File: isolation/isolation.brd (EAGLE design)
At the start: 74.5 x 72.7 mm, 81 parts, among them IC1 XTLV61048DBVR, IC2 SN74HC14PWR, IC3 SN74HCS32BQAR, IC4 SN74HCS08DYYR, IC5 FDN359BN, IC6 FDN359BN, IC7 FDN359BN, IC8 FDN359BN, J1 S4B-PH-K-S(LF)(SN), J2 S4B-PH-K-S(LF)(SN), J3 S4B-PH-K-S(LF)(SN), J4 S4B-PH-K-S(LF)(SN), J5 S4B-PH-K-S(LF)(SN)

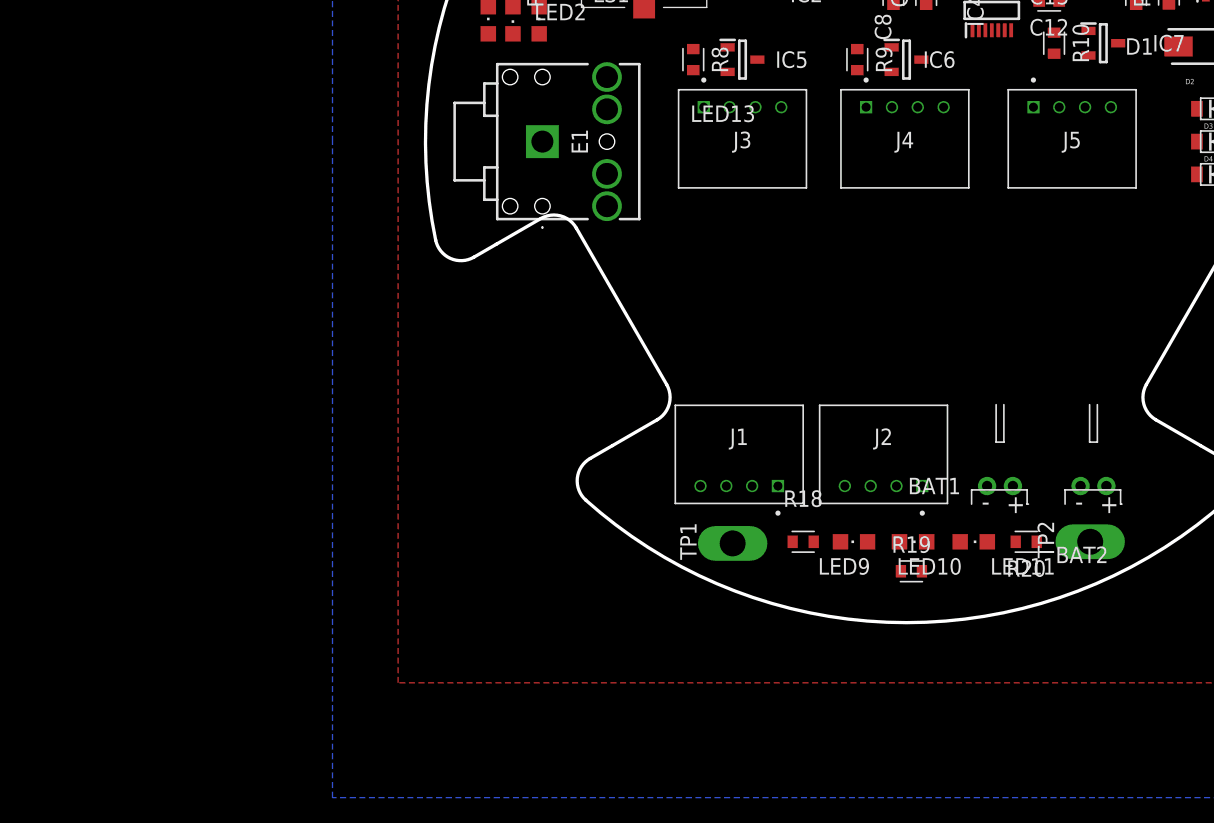
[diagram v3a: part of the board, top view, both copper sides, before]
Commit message: 2 pin ignitor connectors
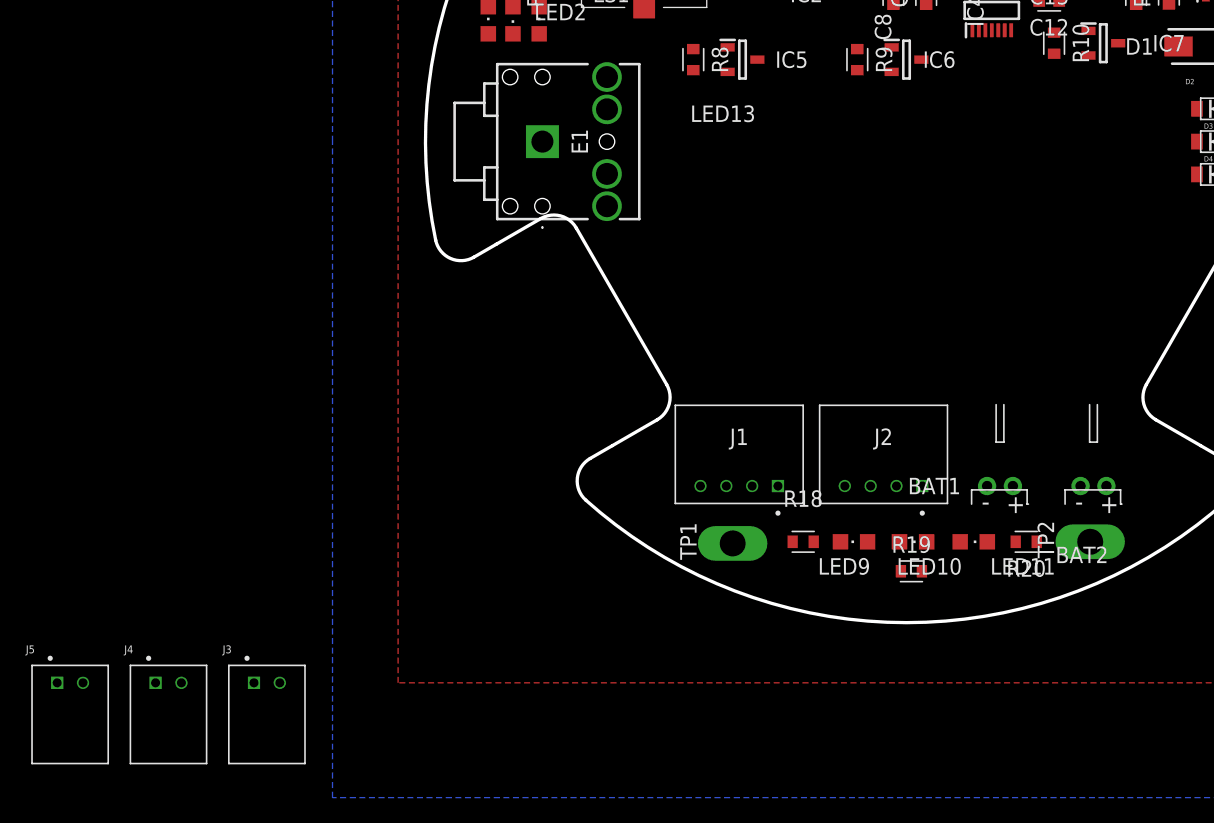
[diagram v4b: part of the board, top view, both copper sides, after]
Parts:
- J3, J4, J5: value S4B-PH-K-S(LF)(SN) -> S2B-PH-K-S(LF)(SN); device Headers:S4B-PH-K-S(LF)(SN) -> Connectors:S2B-PH-K-S(LF)(SN)
- moved J5 89.5 mm to (-64.8, -41.9)
- moved J4 72.4 mm to (-57.1, -41.9)
- moved J3 57.8 mm to (-49.5, -41.9)
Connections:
- removed net N$19: IC6.3, J4.2, J4.3
- removed net N$20: IC7.3, J5.2, J5.3
- new net N$14: IC7.3, J5.2
- new net N$15: IC6.3, J4.2
- net N$17: no longer J3.3
- net VDEP: no longer J3.4, J4.4, J5.4
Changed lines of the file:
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@@
 <attribute name="VALUE" x="-20.32" y="25.4" size="1.27" layer="27" rot="R180" align="center"/>
-</element>
-<element name="J3" library="Headers" library_urn="urn:adsk.eagle:library:11687645" package="S4B-PH-K-S(LF)(SN)" package3d_urn="urn:adsk.eagle:package:19181369/5" value="S4B-PH-K-S(LF)(SN)" x="-12.7" y="2.667" smashed="yes">
-<attribute name="CREATED_BY" value="PCBLayout.com" x="-12.7" y="2.667" size="1.778" layer="27" display="off"/>
-<attribute name="DIGIKEY_PARTNO" value="455-1721-ND" x="-12.7" y="2.667" size="1.778" layer="27" display="off"/>
-<attribute name="MANUFACTURER" value="JST Sales America Inc." x="-12.7" y="2.667" size="1.778" layer="27" display="off"/>
-<attribute name="MPN" value="S4B-PH-K-S(LF)(SN)" x="-12.7" y="2.667" size="1.778" layer="27" display="off"/>
-<attribute name="NAME" x="-12.700003125" y="0.127003125" size="1.27" layer="25" align="center"/>
-<attribute name="VALUE" x="-12.7" y="2.667" size="1.27" layer="27" align="center"/>
-</element>
-<element name="J4" library="Headers" library_urn="urn:adsk.eagle:library:11687645" package="S4B-PH-K-S(LF)(SN)" package3d_urn="urn:adsk.eagle:package:19181369/5" value="S4B-PH-K-S(LF)(SN)" x="-0.127" y="2.667" smashed="yes">
-<attribute name="CREATED_BY" value="PCBLayout.com" x="-0.127" y="2.667" size="1.778" layer="27" display="off"/>
-<attribute name="DIGIKEY_PARTNO" value="455-1721-ND" x="-0.127" y="2.667" size="1.778" layer="27" display="off"/>
-<attribute name="MANUFACTURER" value="JST Sales America Inc." x="-0.127" y="2.667" size="1.778" layer="27" display="off"/>
-<attribute name="MPN" value="S4B-PH-K-S(LF)(SN)" x="-0.127" y="2.667" size="1.778" layer="27" display="off"/>
-<attribute name="NAME" x="-0.127003125" y="0.127003125" size="1.27" layer="25" align="center"/>
-<attribute name="VALUE" x="-0.127" y="2.667" size="1.27" layer="27" align="center"/>
-</element>
-<element name="J5" library="Headers" library_urn="urn:adsk.eagle:library:11687645" package="S4B-PH-K-S(LF)(SN)" package3d_urn="urn:adsk.eagle:package:19181369/5" value="S4B-PH-K-S(LF)(SN)" x="12.827" y="2.667" smashed="yes">
-<attribute name="CREATED_BY" value="PCBLayout.com" x="12.827" y="2.667" size="1.778" layer="27" display="off"/>
-<attribute name="DIGIKEY_PARTNO" value="455-1721-ND" x="12.827" y="2.667" size="1.778" layer="27" display="off"/>
-<attribute name="MANUFACTURER" value="JST Sales America Inc." x="12.827" y="2.667" size="1.778" layer="27" display="off"/>
-<attribute name="MPN" value="S4B-PH-K-S(LF)(SN)" x="12.827" y="2.667" size="1.778" layer="27" display="off"/>
-<attribute name="NAME" x="12.826996875" y="0.127003125" size="1.27" layer="25" align="center"/>
-<attribute name="VALUE" x="12.827" y="2.667" size="1.27" layer="27" align="center"/>
 </element>
 <element name="R8" library="Resistor" library_urn="urn:adsk.eagle:library:16378527" package="RESC1608X60" package3d_urn="urn:adsk.eagle:package:16378565/5" value="68k" x="-16.51" y="6.35" smashed="yes" rot="R270">
@@
 <attribute name="TP_SIGNAL_NAME" value="" x="14.224" y="-30.988" size="1.778" layer="27" font="vector" rot="R90" display="off"/>
 <attribute name="VALUE" x="14.224" y="-30.988" size="0.0254" layer="27" rot="R90"/>
+</element>
+<element name="J3" library="Connectors" library_urn="urn:adsk.eagle:library:14555660" package="S2B-PH-K-S(LF)(SN)" package3d_urn="urn:adsk.eagle:package:10989924/2" value="S2B-PH-K-S(LF)(SN)" x="-49.53" y="-41.91" smashed="yes">
+<attribute name="CREATED_BY" value="PCBLayout.com" x="-49.53" y="-41.91" size="1.778" layer="27" display="off"/>
+<attribute name="DIGI_KEY_PART_NUMBER" value="455-1719-ND" x="-49.53" y="-41.91" size="1.778" layer="27" display="off"/>
+<attribute name="MANUFACTURER" value="JST Sales America Inc." x="-49.53" y="-41.91" size="1.778" layer="27" display="off"/>
+<attribute name="MPN" value="S2B-PH-K-S(LF)(SN)" x="-49.53" y="-41.91" size="1.778" layer="27" display="off"/>
+<attribute name="NAME" x="-52.959" y="-39.624" size="0.6096" layer="25"/>
+<attribute name="VALUE" x="-52.83" y="-49.11" size="0.6096" layer="27"/>
+</element>
+<element name="J4" library="Connectors" library_urn="urn:adsk.eagle:library:14555660" package="S2B-PH-K-S(LF)(SN)" package3d_urn="urn:adsk.eagle:package:10989924/2" value="S2B-PH-K-S(LF)(SN)" x="-57.15" y="-41.91" smashed="yes">
+<attribute name="CREATED_BY" value="PCBLayout.com" x="-57.15" y="-41.91" size="1.778" layer="27" display="off"/>
+<attribute name="DIGI_KEY_PART_NUMBER" value="455-1719-ND" x="-57.15" y="-41.91" size="1.778" layer="27" display="off"/>
+<attribute name="MANUFACTURER" value="JST Sales America Inc." x="-57.15" y="-41.91" size="1.778" layer="27" display="off"/>
+<attribute name="MPN" value="S2B-PH-K-S(LF)(SN)" x="-57.15" y="-41.91" size="1.778" layer="27" display="off"/>
+<attribute name="NAME" x="-60.579" y="-39.624" size="0.6096" layer="25"/>
+<attribute name="VALUE" x="-60.45" y="-49.11" size="0.6096" layer="27"/>
+</element>
+<element name="J5" library="Connectors" library_urn="urn:adsk.eagle:library:14555660" package="S2B-PH-K-S(LF)(SN)" package3d_urn="urn:adsk.eagle:package:10989924/2" value="S2B-PH-K-S(LF)(SN)" x="-64.77" y="-41.91" smashed="yes">
+<attribute name="CREATED_BY" value="PCBLayout.com" x="-64.77" y="-41.91" size="1.778" layer="27" display="off"/>
+<attribute name="DIGI_KEY_PART_NUMBER" value="455-1719-ND" x="-64.77" y="-41.91" size="1.778" layer="27" display="off"/>
+<attribute name="MANUFACTURER" value="JST Sales America Inc." x="-64.77" y="-41.91" size="1.778" layer="27" display="off"/>
+<attribute name="MPN" value="S2B-PH-K-S(LF)(SN)" x="-64.77" y="-41.91" size="1.778" layer="27" display="off"/>
+<attribute name="NAME" x="-68.199" y="-39.624" size="0.6096" layer="25"/>
+<attribute name="VALUE" x="-68.07" y="-49.11" size="0.6096" layer="27"/>
 </element>
 </elements>
@@
 <contactref element="R2" pad="1"/>
 <contactref element="LS1" pad="1"/>
-<contactref element="J3" pad="4"/>
 <contactref element="J3" pad="1"/>
-<contactref element="J4" pad="4"/>
-<contactref element="J5" pad="4"/>
+<contactref element="J4" pad="1"/>
 <contactref element="J5" pad="1"/>
-<contactref element="J4" pad="1"/>
-<wire x1="17.78" y1="10.6554" x2="20.32" y2="10.6148" width="0" layer="19" extent="1-1"/>
+<wire x1="-58.15" y1="-41.91" x2="-65.77" y2="-41.91" width="0" layer="19" extent="1-1"/>
+<wire x1="-50.53" y1="-41.91" x2="-58.15" y2="-41.91" width="0" layer="19" extent="1-1"/>
+<wire x1="-20.32" y1="10.29" x2="-50.53" y2="-41.91" width="0" layer="19" extent="1-1"/>
+<wire x1="17.78" y1="10.6554" x2="-20.32" y2="10.29" width="0" layer="19" extent="1-1"/>
+<wire x1="20.32" y1="10.6148" x2="17.78" y2="10.6554" width="0" layer="19" extent="1-1"/>
 <wire x1="21.064" y1="7.366" x2="20.32" y2="10.6148" width="0" layer="19" extent="1-1"/>
-<wire x1="15.827" y1="2.667" x2="21.064" y2="7.366" width="0" layer="19" extent="1-1"/>
-<wire x1="9.827" y1="2.667" x2="15.827" y2="2.667" width="0" layer="19" extent="1-1"/>
-<wire x1="2.873" y1="2.667" x2="9.827" y2="2.667" width="0" layer="19" extent="1-1"/>
-<wire x1="-3.127" y1="2.667" x2="2.873" y2="2.667" width="0" layer="19" extent="1-1"/>
-<wire x1="-9.7" y1="2.667" x2="-3.127" y2="2.667" width="0" layer="19" extent="1-1"/>
-<wire x1="-15.7" y1="2.667" x2="-9.7" y2="2.667" width="0" layer="19" extent="1-1"/>
-<wire x1="-20.32" y1="10.29" x2="-15.7" y2="2.667" width="0" layer="19" extent="1-1"/>
 </signal>
 <signal name="N$3">
@@
 <contactref element="IC5" pad="3"/>
 <contactref element="J3" pad="2"/>
-<contactref element="J3" pad="3"/>
-<wire x1="-11.7" y1="2.667" x2="-13.7" y2="2.667" width="0" layer="19" extent="1-1"/>
-<wire x1="-11.55" y1="6.35" x2="-11.7" y2="2.667" width="0" layer="19" extent="1-1"/>
-</signal>
-<signal name="N$19">
-<contactref element="IC6" pad="3"/>
-<contactref element="J4" pad="2"/>
-<contactref element="J4" pad="3"/>
-<wire x1="0.873" y1="2.667" x2="1.15" y2="6.35" width="0" layer="19" extent="1-1"/>
-<wire x1="-1.127" y1="2.667" x2="0.873" y2="2.667" width="0" layer="19" extent="1-1"/>
-</signal>
-<signal name="N$20">
-<contactref element="IC7" pad="3"/>
-<contactref element="J5" pad="2"/>
-<contactref element="J5" pad="3"/>
-<wire x1="13.827" y1="2.667" x2="16.39" y2="7.62" width="0" layer="19" extent="1-1"/>
-<wire x1="11.827" y1="2.667" x2="13.827" y2="2.667" width="0" layer="19" extent="1-1"/>
+<wire x1="-11.55" y1="6.35" x2="-48.53" y2="-41.91" width="0" layer="19" extent="1-1"/>
 </signal>
 <signal name="N$22">
@@
 <wire x1="26.67" y1="17.3252" x2="24.785325" y2="21.065" width="0" layer="19" extent="1-1"/>
 </signal>
+<signal name="N$14">
+<contactref element="J5" pad="2"/>
+<contactref element="IC7" pad="3"/>
+<wire x1="16.39" y1="7.62" x2="-63.77" y2="-41.91" width="0" layer="19" extent="1-1"/>
+</signal>
+<signal name="N$15">
+<contactref element="J4" pad="2"/>
+<contactref element="IC6" pad="3"/>
+<wire x1="1.15" y1="6.35" x2="-56.15" y2="-41.91" width="0" layer="19" extent="1-1"/>
+</signal>
 </signals>

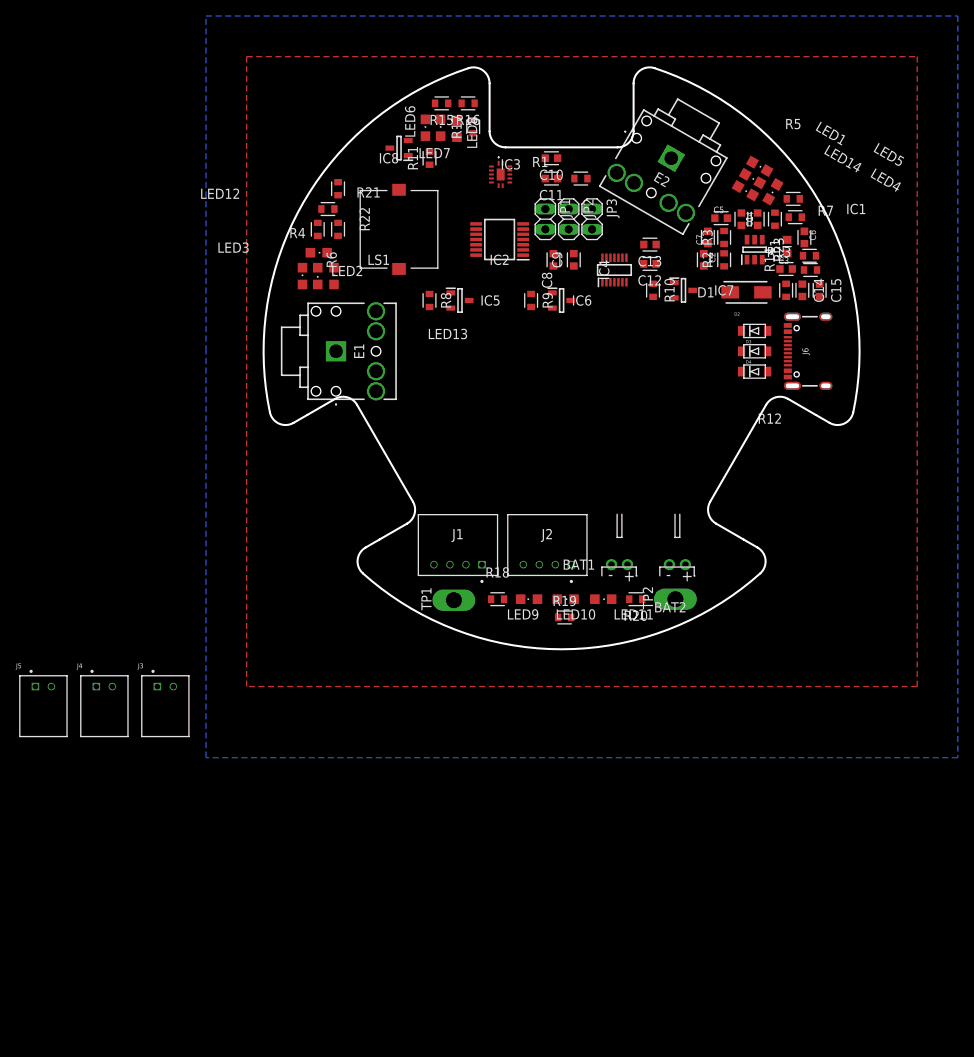
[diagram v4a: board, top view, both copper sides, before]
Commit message: add test pads
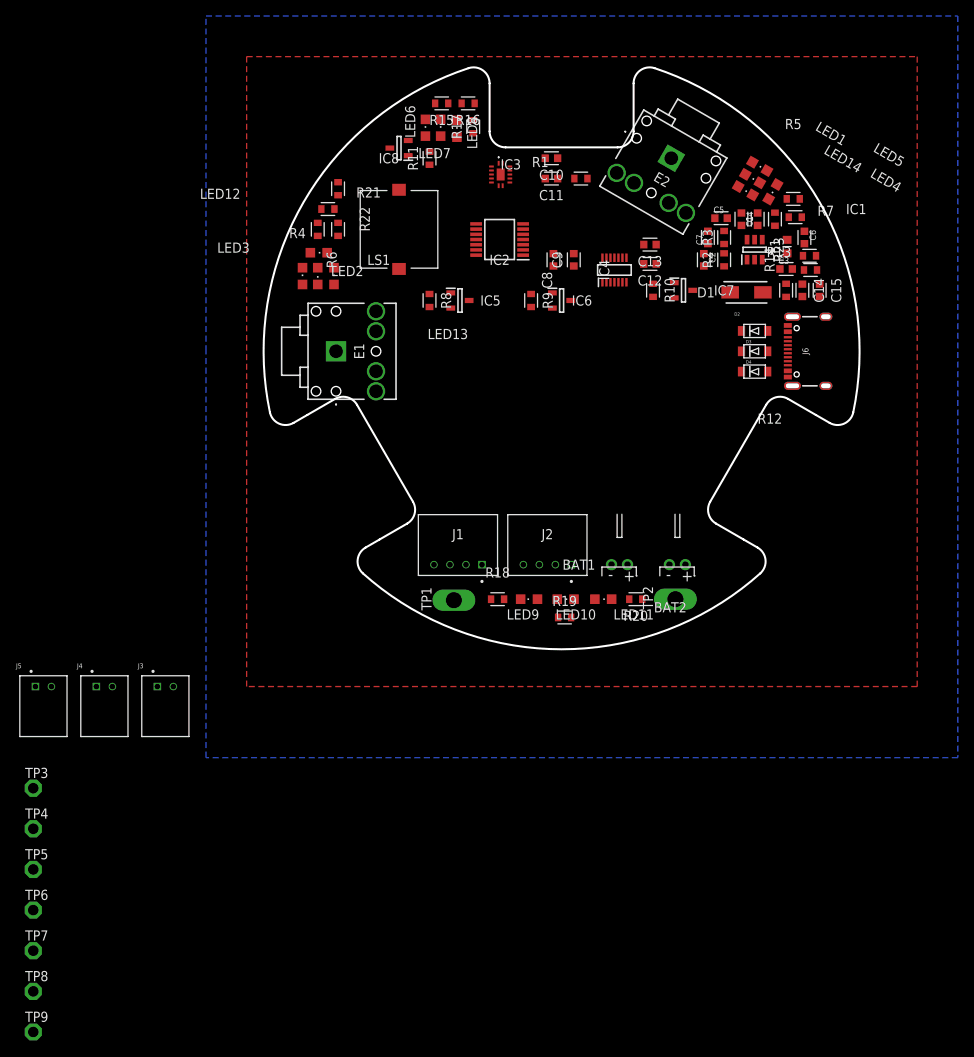
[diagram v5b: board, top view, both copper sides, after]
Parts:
- removed JP1, JP2, JP3: (no value), pinhead:1X02
- added TP3, TP4, TP5, TP6, TP7, TP8, TP9: PTR1PAD1-13, testpad:P1-13
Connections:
- net FIRE1: now also TP4.TP; no longer JP1.1
- net FIRE2: now also TP6.TP; no longer JP2.1
- net FIRE3: now also TP8.TP; no longer JP3.1
- net VBAT: now also TP3.TP, TP5.TP, TP7.TP; no longer JP1.2, JP2.2, JP3.2
- net VDEP: now also TP9.TP

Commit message: placed shrunken components
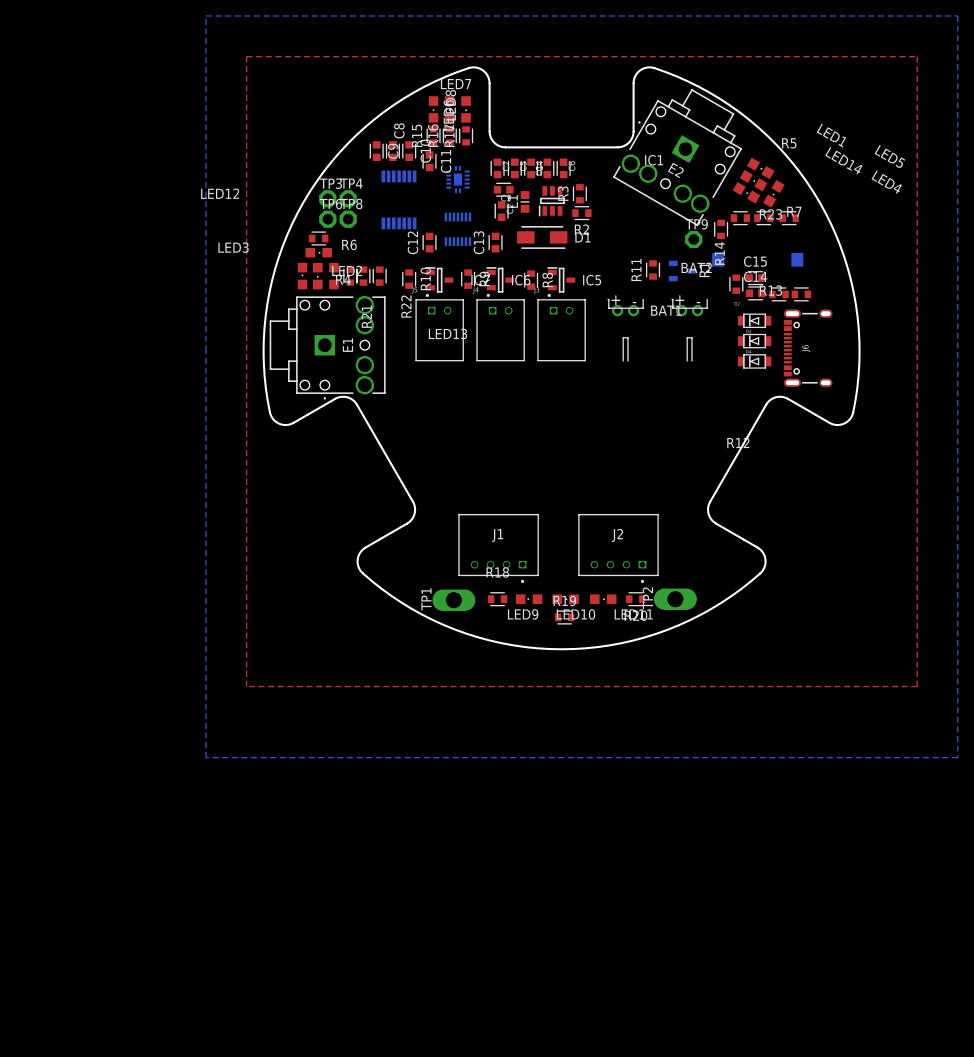
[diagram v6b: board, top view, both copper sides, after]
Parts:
- removed TP5, TP7: PTR1PAD1-13, testpad:P1-13
- moved TP9 128.9 mm to (16.5, 14.0)
- moved TP8 104.2 mm to (-26.7, 16.5)
- moved TP6 93.9 mm to (-29.2, 16.5)
- moved TP4 88.0 mm to (-26.7, 19.1)
- moved TP3 82.4 mm to (-29.2, 19.1)
- moved J3 68.3 mm to (0.00, 5.08)
- moved J4 68.3 mm to (-7.62, 5.08)
- moved J5 68.3 mm to (-15.2, 5.08)
- moved LS1 45.0 mm to (24.5, 11.4), flipped to the bottom, turned to 270 degrees
- moved IC8 38.6 mm to (15.1, 10.0), flipped to the bottom
- moved C3 36.7 mm to (-7.24, 20.2), turned to 180 degrees
- moved L1 33.2 mm to (-4.57, 18.7)
- moved BAT2 31.8 mm to (16.0, 5.08), turned to 180 degrees
- moved BAT1 31.8 mm to (8.00, 5.08), turned to 180 degrees
- moved C6 31.3 mm to (0.25, 22.9)
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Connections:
- net VBAT: no longer TP5.TP, TP7.TP

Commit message: central cutout
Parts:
- moved IC5 15.2 mm to (-15.2, 8.89)
- moved IC7 15.2 mm to (0.00, 8.89)
- moved J3 15.2 mm to (-15.2, 5.08)
- moved J5 15.2 mm to (0.00, 5.08)
- moved R10 15.2 mm to (-3.81, 9.02)
- moved R8 15.2 mm to (-19.1, 8.89)
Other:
- outline, holes or cut-outs redrawn

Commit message: final routing
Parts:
- moved D3 1.15 mm to (23.0, 1.14)
- moved D2 1.14 mm to (23.0, 3.81)
- moved D4 1.14 mm to (23.0, -1.27)
- moved TP3 0.76 mm to (-28.4, 19.1)
- moved TP4 0.76 mm to (-25.9, 19.1)
- moved TP6 0.76 mm to (-28.4, 16.5)
- moved TP8 0.76 mm to (-25.9, 16.5)
- moved R14 0.40 mm to (21.5, 8.26)
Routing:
- net EN1: track 0.00 -> 88.6 mm, vias 0 -> 10
- net PICKLE1: track 0.00 -> 87.1 mm, vias 0 -> 3
- net PICKLE3: track 0.00 -> 84.3 mm, vias 0 -> 5
- net GND: track 0.00 -> 83.9 mm, vias 0 -> 18
- net PICKLE2: track 0.00 -> 83.5 mm, vias 0 -> 3
- net FIRE3: track 0.00 -> 80.7 mm, vias 0 -> 5
- net EN2: track 0.00 -> 74.8 mm, vias 0 -> 10
- net VDEP: track 0.00 -> 72.5 mm
- net RAVEN3: track 0.00 -> 64.2 mm, vias 0 -> 7
- net SAFE2: track 0.00 -> 62.5 mm, vias 0 -> 3
- net RAVEN2: track 0.00 -> 52.1 mm, vias 0 -> 5
- net VBAT: track 0.00 -> 51.6 mm, vias 0 -> 13
- net RAVEN1: track 0.00 -> 48.0 mm, vias 0 -> 3
- net BUZZ: track 0.00 -> 41.4 mm, vias 0 -> 4
- net FIRE2: track 0.00 -> 38.0 mm, vias 0 -> 2
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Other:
- outline, holes or cut-outs redrawn
